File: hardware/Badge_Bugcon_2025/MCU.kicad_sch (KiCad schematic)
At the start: 64 parts, among them J1 Flash, J11 CODEC, J13 ETH, J14 +1V8, J2 Conn_01x04, J5 3V3, J8 3V3, SW2 SW_Push, SW3 SW_Push, U6 W25N02KVZEIR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

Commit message: feat(Hw):Init_Route
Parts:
- removed J1: Flash, Connector_PinHeader_2.54mm:PinHeader_1x08_P2.54mm_Vertical, symbol Connector_Generic:Conn_01x08
- removed J11: CODEC, symbol Connector_Generic:Conn_01x09
- removed J2: Conn_01x04, Connector_PinHeader_2.54mm:PinHeader_1x04_P2.54mm_Vertical, symbol Connector_Generic:Conn_01x04
- added J1: Conn_01x21, Connector_PinHeader_2.54mm:PinHeader_1x21_P2.54mm_Vertical, symbol Connector_Generic:Conn_01x21
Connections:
- net +1V8: now also J1.1 (Pin_1)
- net +3V3: now also J1.10 (Pin_10), J1.18 (Pin_18)
- net CODEC_LINEOUT: now also J1.2 (Pin_2)
- net CODEC_MIC0N: now also J1.4 (Pin_4)
- net CODEC_MIC0P: now also J1.5 (Pin_5)
- net CODEC_MIC1N: now also J1.6 (Pin_6)
- net CODEC_MIC1P: now also J1.7 (Pin_7)
- net CODEC_MICBIAS: now also J1.3 (Pin_3)
- net DEBUG_RX: now also J1.20 (Pin_20)
- net DEBUG_TX: now also J1.19 (Pin_19)
- net FSPI_CS0N: now also J1.14 (Pin_14)
- net FSPI_D0: now also J1.13 (Pin_13)
- net FSPI_D1: now also J1.15 (Pin_15)
- net FSPI_D2: now also J1.16 (Pin_16)
- net FSPI_D3: now also J1.11 (Pin_11)
- net FSPI_SCK: now also J1.12 (Pin_12)
- net GND: now also J1.17 (Pin_17), J1.21 (Pin_21), J1.8 (Pin_8), J1.9 (Pin_9)
- net GPIO3_C4_D: now also J14.10 (Pin_10); no longer J14.2 (Pin_2)
- net GPIO3_C5_D: now also J14.9 (Pin_9); no longer J14.3 (Pin_3)
- net GPIO3_C7_D: now also J14.7 (Pin_7); no longer J14.5 (Pin_5)
- net GPIO3_D0_D: now also J14.5 (Pin_5); no longer J14.7 (Pin_7)
- net GPIO3_D2_D: now also J14.4 (Pin_4); no longer J14.8 (Pin_8)
- net GPIO3_D3_D: now also J14.3 (Pin_3); no longer J14.9 (Pin_9)
- net GPIO4_C1_Z: now also J14.2 (Pin_2); no longer J14.10 (Pin_10)
- net LED: now also J14.8 (Pin_8); no longer J14.4 (Pin_4)
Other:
- moved on the sheet: J13, J14

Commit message: feat(Hw):Update_Route
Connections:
- net CODEC_LINEOUT: now also J1.8 (Pin_8); no longer J1.2 (Pin_2)
- net GND: no longer J1.8 (Pin_8)
- net CODEC_VCM: now reaches C1.1, U8.30 (CODEC_VCM)
- net CODEC_VCM: now also J1.2 (Pin_2)
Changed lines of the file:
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@@
+		)
+	)
+	(label "CODEC_VCM"
+		(at 133.35 93.98 0)
+		(effects
+			(font
+				(size 1.27 1.27)
+			)
+			(justify left bottom)
 		)
 	)
@@
 		)
 	)
-	(label "CODEC_AVSS"
-		(at 151.13 129.54 0)
-		(effects
-			(font
-				(size 1.27 1.27)
-			)
-			(justify left bottom)
-		)
-	)
 	(label "GPIO2_A_2_D"
 		(at 289.56 156.21 180)
@@
 		)
 	)
-	(label "CODEC_AVSS"
-		(at 48.26 236.22 0)
-		(effects
-			(font
-				(size 1.27 1.27)
-			)
-			(justify left bottom)
-		)
-	)
 	(label "GPIO2_B1_D_2"
 		(at 289.56 140.97 180)
@@
 	)
 	(label "CODEC_LINEOUT"
-		(at 48.26 220.98 0)
+		(at 48.26 236.22 0)
 		(effects
 			(font
@@
 		(effects
 			(font
+				(size 1.27 1.27)
+			)
+			(justify left bottom)
+		)
+	)
+	(label "CODEC_VCM"
+		(at 48.26 220.98 0)
+		(effects
+			(font

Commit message: feat(Hw):Update_Route
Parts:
- removed J14: +1V8, Connector_PinHeader_2.54mm:PinHeader_1x23_P2.54mm_Vertical, symbol Connector_Generic:Conn_01x23
- removed J8: 3V3, Connector_PinSocket_2.54mm:PinSocket_1x23_P2.54mm_Vertical, symbol Connector_Generic:Conn_01x23
- added J14, J8: Conn_01x24, Connector_PinSocket_2.54mm:PinSocket_1x24_P2.54mm_Vertical, symbol Connector_Generic:Conn_01x24
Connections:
- net +1V8: now also J1.9 (Pin_9), J14.12 (Pin_12), J8.12 (Pin_12); no longer J1.1 (Pin_1)
- net +3V3: now also J5.24 (Pin_24), J14.24 (Pin_24), J8.1 (Pin_1); no longer J5.1 (Pin_1)
- net GND: now also J1.1 (Pin_1), J5.1 (Pin_1), J14.1 (Pin_1), J8.24 (Pin_24); no longer J1.9 (Pin_9), J5.24 (Pin_24)
- net GPIO1_C0_D: now also J14.18 (Pin_18)
- net GPIO1_C1_D: now also J8.6 (Pin_6)
- net GPIO1_C3_D: now also J14.19 (Pin_19)
- net GPIO1_C4_D: now also J8.5 (Pin_5)
- net GPIO1_C5_D: now also J14.20 (Pin_20)
- net GPIO1_C6_D: now also J14.23 (Pin_23)
- net GPIO1_C7_D: now also J8.2 (Pin_2)
- net GPIO1_D0_D: now also J8.4 (Pin_4)
- net GPIO1_D1_D: now also J14.21 (Pin_21)
- net GPIO1_D2_D: now also J8.3 (Pin_3)
- net GPIO1_D3_D: now also J14.22 (Pin_22)
- net GPIO2_A0_D_1: now also J8.9 (Pin_9)
- net GPIO2_A0_D_2: now also J14.15 (Pin_15)
- net GPIO2_A3_D: now also J8.10 (Pin_10)
- net GPIO2_A4_D: now also J14.13 (Pin_13)
- net GPIO2_A5_D: now also J8.11 (Pin_11)
- net GPIO2_A6_D: now also J14.16 (Pin_16)
- net GPIO2_A7_D: now also J8.8 (Pin_8)
- net GPIO2_A_2_D: now also J14.14 (Pin_14)
- net GPIO2_B1_D_1: now also J8.7 (Pin_7)
- net GPIO2_B1_D_2: now also J14.17 (Pin_17)
- net GPIO3_B0_D: now also J8.13 (Pin_13)
- net GPIO3_B1_D: now also J14.11 (Pin_11)
- net GPIO3_B2_D: now also J8.14 (Pin_14)
- net GPIO3_B3_D: now also J14.10 (Pin_10)
- net GPIO3_B4_D: now also J8.15 (Pin_15)
- net GPIO3_B5_D: now also J14.9 (Pin_9)
- net GPIO3_B6_D: now also J8.16 (Pin_16)
- net GPIO3_B7_D: now also J14.8 (Pin_8)
- net GPIO3_C0_D: now also J8.17 (Pin_17)
- net GPIO3_C1_D: now also J14.7 (Pin_7)
- net GPIO3_C2_D: now also J8.18 (Pin_18)
- net GPIO3_C3_D: now also J14.6 (Pin_6)
- net GPIO3_C4_D: now also J8.19 (Pin_19)
- net GPIO3_C5_D: now also J14.5 (Pin_5)
- net GPIO3_C7_D: now also J14.4 (Pin_4)
- net GPIO3_D0_D: now also J14.3 (Pin_3)
- net GPIO3_D1_D: now also J8.21 (Pin_21)
- net GPIO3_D2_D: now also J8.22 (Pin_22)
- net GPIO3_D3_D: now also J14.2 (Pin_2)
- net GPIO4_C1_Z: now also J8.23 (Pin_23)
- net LED: now also J8.20 (Pin_20)
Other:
- moved on the sheet: J1, J13, J5

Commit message: feat(hw):Updated_review
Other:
- note removed: "SERIAL PORT"
- moved on the sheet: C20, C23, C24, C25, C26, C27, C28, C29, C3, C30, C34, C35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

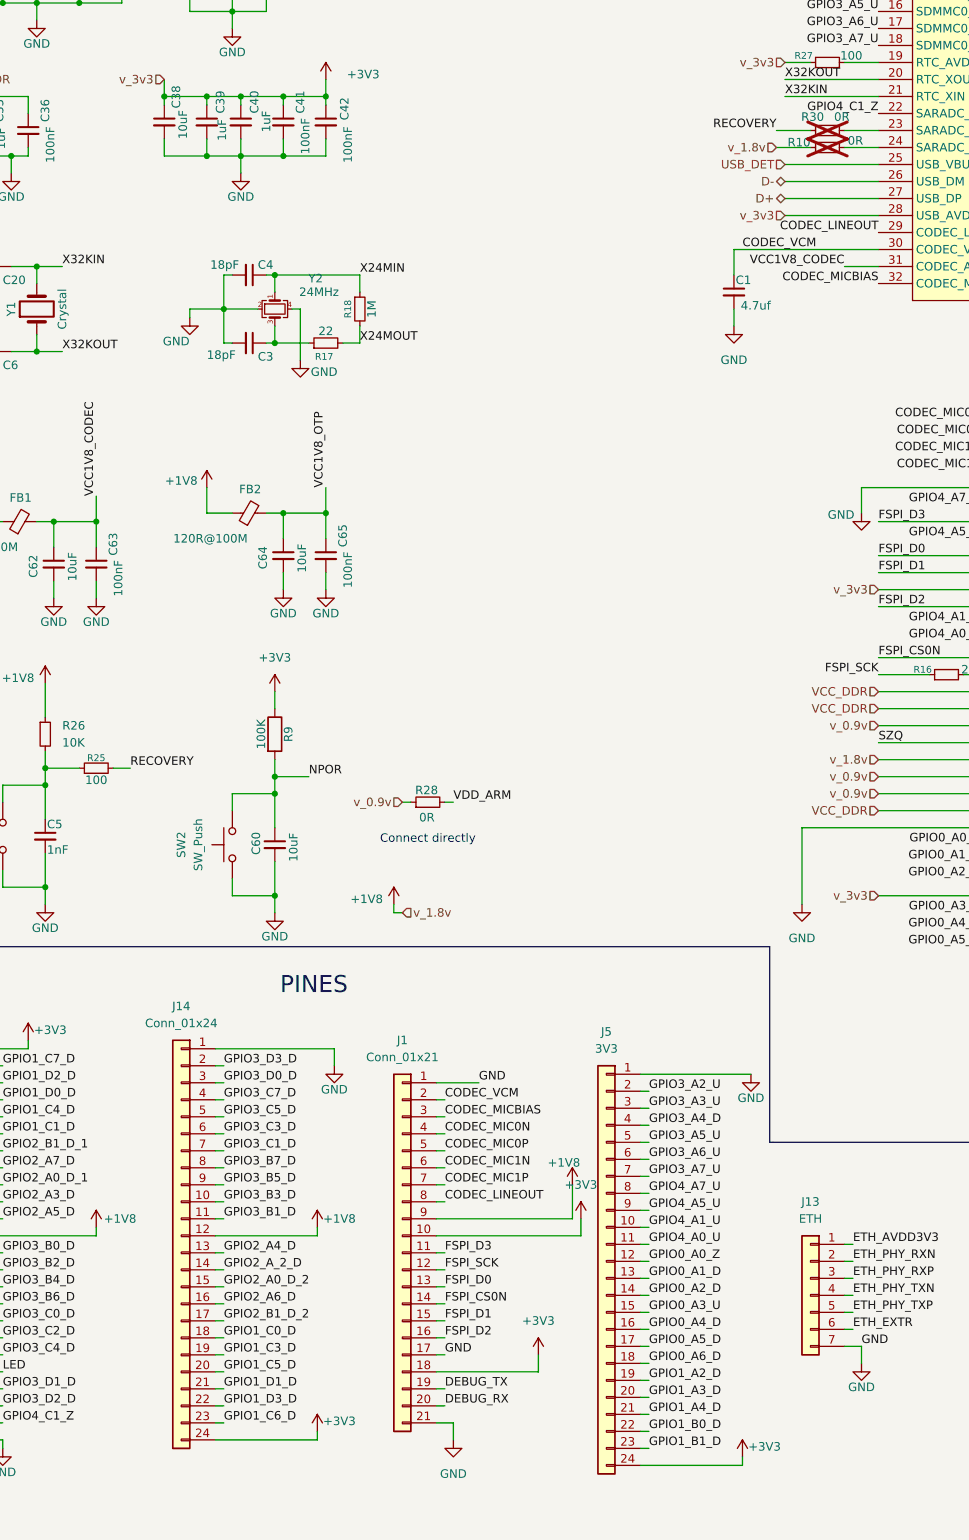
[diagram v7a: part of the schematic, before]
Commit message: feat(Hw):Update_BOM_And_Labels
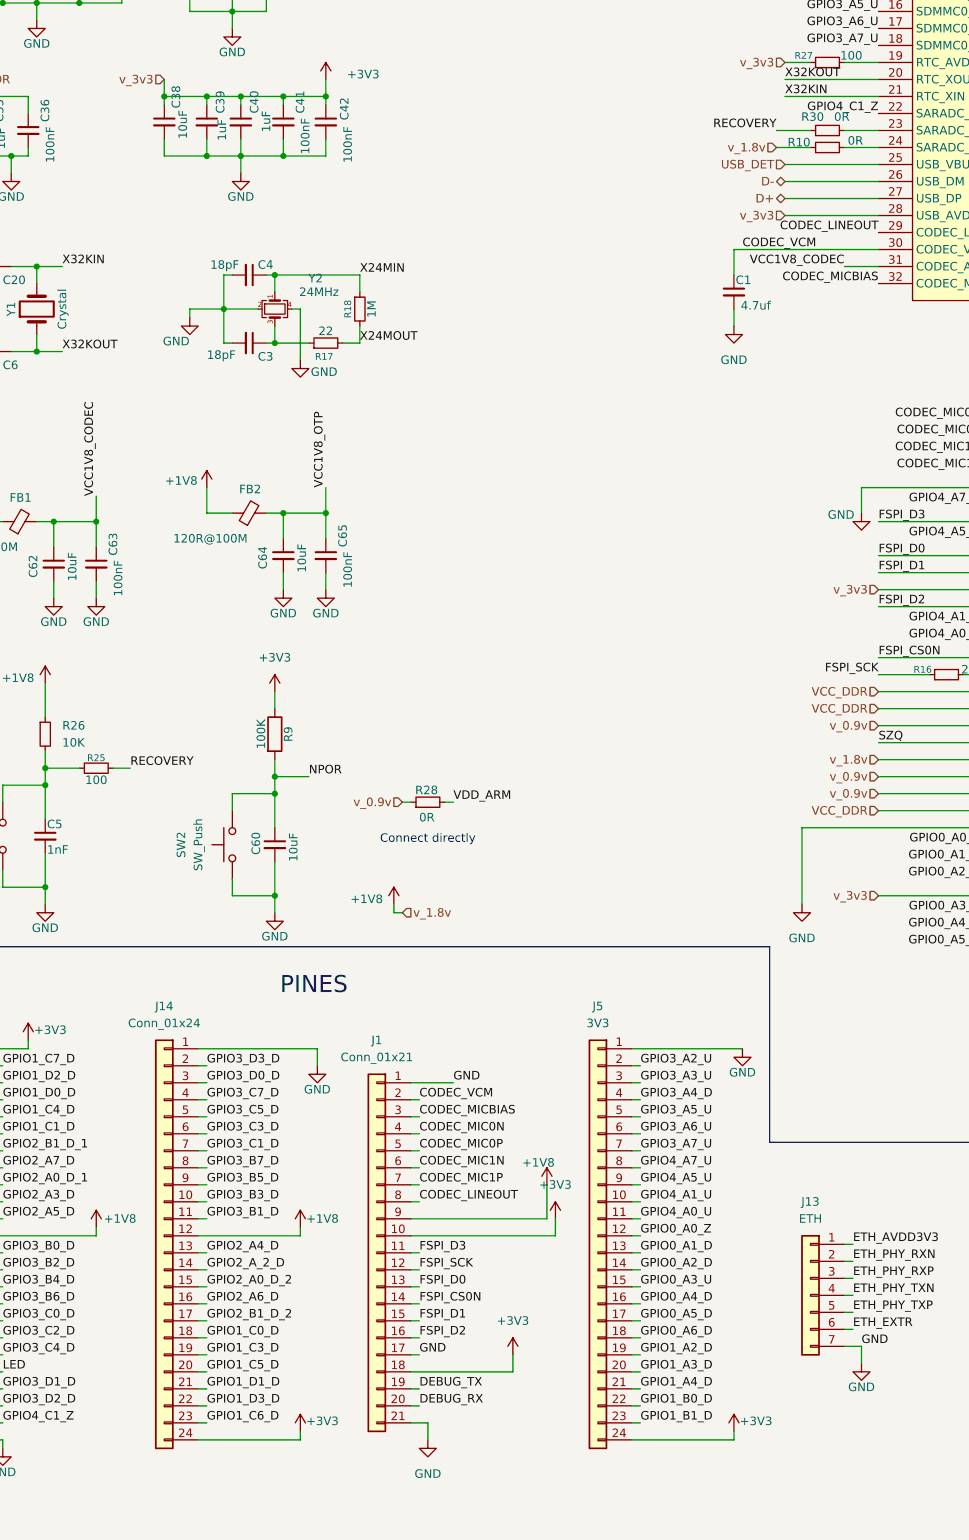
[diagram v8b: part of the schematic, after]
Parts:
- J14, J5, J8: footprint Connector_PinSocket_2.54mm:PinSocket_1x24_P2.54mm_Vertical -> Connector_PinHeader_2.54mm:PinHeader_1x24_P2.54mm_Vertical
- R10, R30: LCSC# (none) -> C106231; now fitted
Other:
- moved on the sheet: J1, J14, J5
